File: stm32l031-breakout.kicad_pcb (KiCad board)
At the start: 2 copper layers, 12 parts, among them J1 Conn_01x16, J2 Conn_01x16, U1 STM32L031K6Tx

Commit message: Placement candidate
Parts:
- moved C6 9.09 mm to (143.5, 113.7), turned to 90 degrees
- moved R1 4.62 mm to (143.5, 109.9), turned to 270 degrees
- moved C4 3.64 mm to (146.7, 118.6), turned to 180 degrees
- moved J2 2.54 mm to (139.7, 104.1)
- moved SW_BOOT1 1.91 mm to (146.7, 111.8)
- moved C1 1.42 mm to (152.4, 112.4)
- moved U1 1.42 mm to (160.0, 112.4)
- moved C2 1.42 mm to (167.6, 112.4)
- moved C3 1.28 mm to (154.2, 117.2)
- moved SW_RST1 0.64 mm to (140.3, 111.8), turned to 270 degrees
- moved C5 0.25 mm to (141.0, 119.1)
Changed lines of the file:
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@@
   )
   (module local_footprints:0805_HS (layer F.Cu)
-    (at 151.13 111.76 90)
+    (at 152.4 112.395 90)
     (descr "Resistor SMD 0805, reflow soldering, Vishay (see dcrcw.pdf)")
     (tags "resistor 0805")
@@
   )
   (module local_footprints:0805_HS (layer F.Cu)
-    (at 166.37 111.76 270)
+    (at 167.64 112.395 270)
     (descr "Resistor SMD 0805, reflow soldering, Vishay (see dcrcw.pdf)")
     (tags "resistor 0805")
@@
   )
   (module local_footprints:0805_HS (layer F.Cu)
-    (at 153.213173 116.383173 135)
+    (at 154.178 117.221 135)
     (descr "Resistor SMD 0805, reflow soldering, Vishay (see dcrcw.pdf)")
     (tags "resistor 0805")
@@
   )
   (module local_footprints:1206_HS (layer F.Cu)
-    (at 149.86 116.84 90)
+    (at 146.685 118.618 180)
     (descr "Resistor SMD 1206, reflow soldering, Vishay (see dcrcw.pdf)")
     (tags "resistor 1206")
     (attr smd)
-    (fp_text reference C4 (at 0 0 180) (layer F.SilkS)
+    (fp_text reference C4 (at 0 0 270) (layer F.SilkS)
       (effects (font (size 0.762 0.762) (thickness 0.1016)))
     )
-    (fp_text value 1uF (at 0 1.95 90) (layer F.Fab) hide
+    (fp_text value 1uF (at 0 1.95 180) (layer F.Fab) hide
       (effects (font (size 1 1) (thickness 0.15)))
     )
@@
     (fp_line (start 1.6 0.8) (end -1.6 0.8) (layer F.Fab) (width 0.1))
     (fp_line (start -1.6 0.8) (end -1.6 -0.8) (layer F.Fab) (width 0.1))
-    (fp_text user %R (at 0 0 90) (layer F.Fab)
+    (fp_text user %R (at 0 0 180) (layer F.Fab)
       (effects (font (size 0.7 0.7) (thickness 0.105)))
     )
-    (pad 2 smd roundrect (at 1.65 0 90) (size 1.3 1.7) (layers F.Cu F.Paste F.Mask) (roundrect_rratio 0.25)
-      (net 2 GND))
-    (pad 1 smd roundrect (at -1.65 0 90) (size 1.3 1.7) (layers F.Cu F.Paste F.Mask) (roundrect_rratio 0.25)
+    (pad 2 smd roundrect (at 1.65 0 180) (size 1.3 1.7) (layers F.Cu F.Paste F.Mask) (roundrect_rratio 0.25)
+      (net 2 GND))
+    (pad 1 smd roundrect (at -1.65 0 180) (size 1.3 1.7) (layers F.Cu F.Paste F.Mask) (roundrect_rratio 0.25)
       (net 1 VDD))
     (model ${KISYS3DMOD}/Resistors_SMD.3dshapes/R_1206.wrl
@@
   )
   (module local_footprints:1210_HS (layer F.Cu)
-    (at 140.97 119.38)
+    (at 140.97 119.126)
     (descr "Generic SMD 1210")
     (tags "resistor 1206")
@@
   )
   (module local_footprints:0805_HS (layer F.Cu)
-    (at 139.7 105.41)
+    (at 143.51 113.665 90)
     (descr "Resistor SMD 0805, reflow soldering, Vishay (see dcrcw.pdf)")
     (tags "resistor 0805")
     (attr smd)
-    (fp_text reference C6 (at 0 0 90) (layer F.SilkS)
+    (fp_text reference C6 (at 0 0 180) (layer F.SilkS)
       (effects (font (size 0.635 0.635) (thickness 0.1016)))
     )
-    (fp_text value 0.1uF (at 0 1.75) (layer F.Fab) hide
-      (effects (font (size 1 1) (thickness 0.15)))
-    )
-    (fp_text user %R (at 0 0) (layer F.Fab)
+    (fp_text value 0.1uF (at 0 1.75 90) (layer F.Fab) hide
+      (effects (font (size 1 1) (thickness 0.15)))
+    )
+    (fp_text user %R (at 0 0 90) (layer F.Fab)
       (effects (font (size 0.5 0.5) (thickness 0.075)))
     )
@@
     (fp_line (start 1.55 0.9) (end 1.55 -0.9) (layer F.CrtYd) (width 0.05))
     (fp_line (start 1.55 0.9) (end -1.55 0.9) (layer F.CrtYd) (width 0.05))
-    (pad 1 smd roundrect (at -1.15 0) (size 1.1 1.3) (layers F.Cu F.Paste F.Mask) (roundrect_rratio 0.25)
+    (pad 1 smd roundrect (at -1.15 0 90) (size 1.1 1.3) (layers F.Cu F.Paste F.Mask) (roundrect_rratio 0.25)
       (net 3 "Net-(C6-Pad1)"))
-    (pad 2 smd roundrect (at 1.15 0) (size 1.1 1.3) (layers F.Cu F.Paste F.Mask) (roundrect_rratio 0.25)
+    (pad 2 smd roundrect (at 1.15 0 90) (size 1.1 1.3) (layers F.Cu F.Paste F.Mask) (roundrect_rratio 0.25)
       (net 2 GND))
     (model ${KISYS3DMOD}/Resistors_SMD.3dshapes/R_0805.wrl
@@
   )
   (module local_footprints:Pin_Header_Straight_1x16_Pitch2.54mm (layer F.Cu)
-    (at 139.7 101.6 90)
+    (at 139.7 104.14 90)
     (descr "Through hole straight pin header, 1x16, 2.54mm pitch, single row")
     (tags "Through hole pin header THT 1x16 2.54mm single row")
@@
   )
   (module local_footprints:0805_HS (layer F.Cu)
-    (at 144.78 105.41 180)
+    (at 143.51 109.855 270)
     (descr "Resistor SMD 0805, reflow soldering, Vishay (see dcrcw.pdf)")
     (tags "resistor 0805")
     (attr smd)
-    (fp_text reference R1 (at 0 0 270) (layer F.SilkS)
+    (fp_text reference R1 (at 0 0) (layer F.SilkS)
       (effects (font (size 0.635 0.635) (thickness 0.1016)))
     )
-    (fp_text value 10k (at 0 1.75 180) (layer F.Fab) hide
+    (fp_text value 10k (at 0 1.75 270) (layer F.Fab) hide
       (effects (font (size 1 1) (thickness 0.15)))
     )
@@
     (fp_line (start 1 0.62) (end -1 0.62) (layer F.Fab) (width 0.1))
     (fp_line (start -1 0.62) (end -1 -0.62) (layer F.Fab) (width 0.1))
-    (fp_text user %R (at 0 0 180) (layer F.Fab)
+    (fp_text user %R (at 0 0 270) (layer F.Fab)
       (effects (font (size 0.5 0.5) (thickness 0.075)))
     )
-    (pad 2 smd roundrect (at 1.15 0 180) (size 1.1 1.3) (layers F.Cu F.Paste F.Mask) (roundrect_rratio 0.25)
-      (net 2 GND))
-    (pad 1 smd roundrect (at -1.15 0 180) (size 1.1 1.3) (layers F.Cu F.Paste F.Mask) (roundrect_rratio 0.25)
+    (pad 2 smd roundrect (at 1.15 0 270) (size 1.1 1.3) (layers F.Cu F.Paste F.Mask) (roundrect_rratio 0.25)
+      (net 2 GND))
+    (pad 1 smd roundrect (at -1.15 0 270) (size 1.1 1.3) (layers F.Cu F.Paste F.Mask) (roundrect_rratio 0.25)
       (net 29 BOOT))
     (model ${KISYS3DMOD}/Resistors_SMD.3dshapes/R_0805.wrl
@@
   )
   (module local_footprints:SW_SPST_PUSH_6mm_3mm (layer F.Cu)
-    (at 144.78 111.76 270)
+    (at 146.685 111.76 270)
     (descr http://www.te.com/commerce/DocumentDelivery/DDEController?Action=srchrtrv&DocNm=1437566-3&DocType=Customer+Drawing&DocLang=English)
     (tags "SPST button tactile switch")
@@
   )
   (module local_footprints:SW_SPST_PUSH_6mm_3mm (layer F.Cu)
-    (at 139.7 111.76 90)
+    (at 140.335 111.76 270)
     (descr http://www.te.com/commerce/DocumentDelivery/DDEController?Action=srchrtrv&DocNm=1437566-3&DocType=Customer+Drawing&DocLang=English)
     (tags "SPST button tactile switch")
     (attr smd)
-    (fp_text reference SW_RST1 (at 0 0 90) (layer F.SilkS)
-      (effects (font (size 1 1) (thickness 0.15)))
-    )
-    (fp_text value SW_RST (at 0 3 90) (layer F.Fab)
+    (fp_text reference SW_RST1 (at 0 0 270) (layer F.SilkS)
+      (effects (font (size 1 1) (thickness 0.15)))
+    )
+    (fp_text value SW_RST (at 0 3 270) (layer F.Fab)
       (effects (font (size 1 1) (thickness 0.15)))
     )
@@
     (fp_line (start 1.75 -1) (end 1.75 1) (layer F.Fab) (width 0.1))
     (fp_line (start -1.75 -1) (end 1.75 -1) (layer F.Fab) (width 0.1))
-    (fp_text user %R (at 0 -2.6 90) (layer F.Fab)
-      (effects (font (size 1 1) (thickness 0.15)))
-    )
-    (pad 2 smd roundrect (at 3.9 0 90) (size 2 1.6) (layers F.Cu F.Paste F.Mask) (roundrect_rratio 0.25)
+    (fp_text user %R (at 0 -2.6 270) (layer F.Fab)
+      (effects (font (size 1 1) (thickness 0.15)))
+    )
+    (pad 2 smd roundrect (at 3.9 0 270) (size 2 1.6) (layers F.Cu F.Paste F.Mask) (roundrect_rratio 0.25)
       (net 3 "Net-(C6-Pad1)"))
-    (pad 1 smd roundrect (at -3.9 0 90) (size 2 1.6) (layers F.Cu F.Paste F.Mask) (roundrect_rratio 0.25)
+    (pad 1 smd roundrect (at -3.9 0 270) (size 2 1.6) (layers F.Cu F.Paste F.Mask) (roundrect_rratio 0.25)
       (net 2 GND))
     (model ${KISYS3DMOD}/Buttons_Switches_SMD.3dshapes/SW_SPST_FSMSM.wrl
@@
   )
   (module local_footprints:TQFP-32_7x7mm_Pitch0.8mm_HS_narrow_pads (layer F.Cu)
-    (at 158.75 111.76 45)
+    (at 160.02 112.395 45)
     (descr "32-Lead Plastic Thin Quad Flatpack (PT) - 7x7x1.0 mm Body, 2.00 mm [TQFP] (see Microchip Packaging Specification 00000049BS.pdf)")
     (tags "QFP 0.8")

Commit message: Full layout
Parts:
- moved C4 2.83 mm to (149.5, 118.2)
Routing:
- net VDD: track 0.00 -> 46.4 mm
- net Net-(C6-Pad1): track 0.00 -> 21.0 mm, vias 0 -> 2
- net GND: track 0.00 -> 20.1 mm, vias 0 -> 9
- net PB1: track 0.00 -> 16.5 mm
- net PB7: track 0.00 -> 16.3 mm
- net PA8: track 0.00 -> 16.0 mm
- net PC14: track 0.00 -> 14.9 mm, vias 0 -> 2
- net PB0: track 0.00 -> 14.3 mm
- net PB6: track 0.00 -> 14.1 mm
- net PA9.SCL.TX: track 0.00 -> 13.8 mm
- net BOOT: track 0.00 -> 13.5 mm
- net PC15: track 0.00 -> 12.7 mm, vias 0 -> 2
- net PB5: track 0.00 -> 11.9 mm
- net PA10.SDA.RX: track 0.00 -> 11.6 mm
- net PA0: track 0.00 -> 10.5 mm
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- added copper zone on B.Cu, net GND
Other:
- board outline added: 40.6 x 20.3 mm

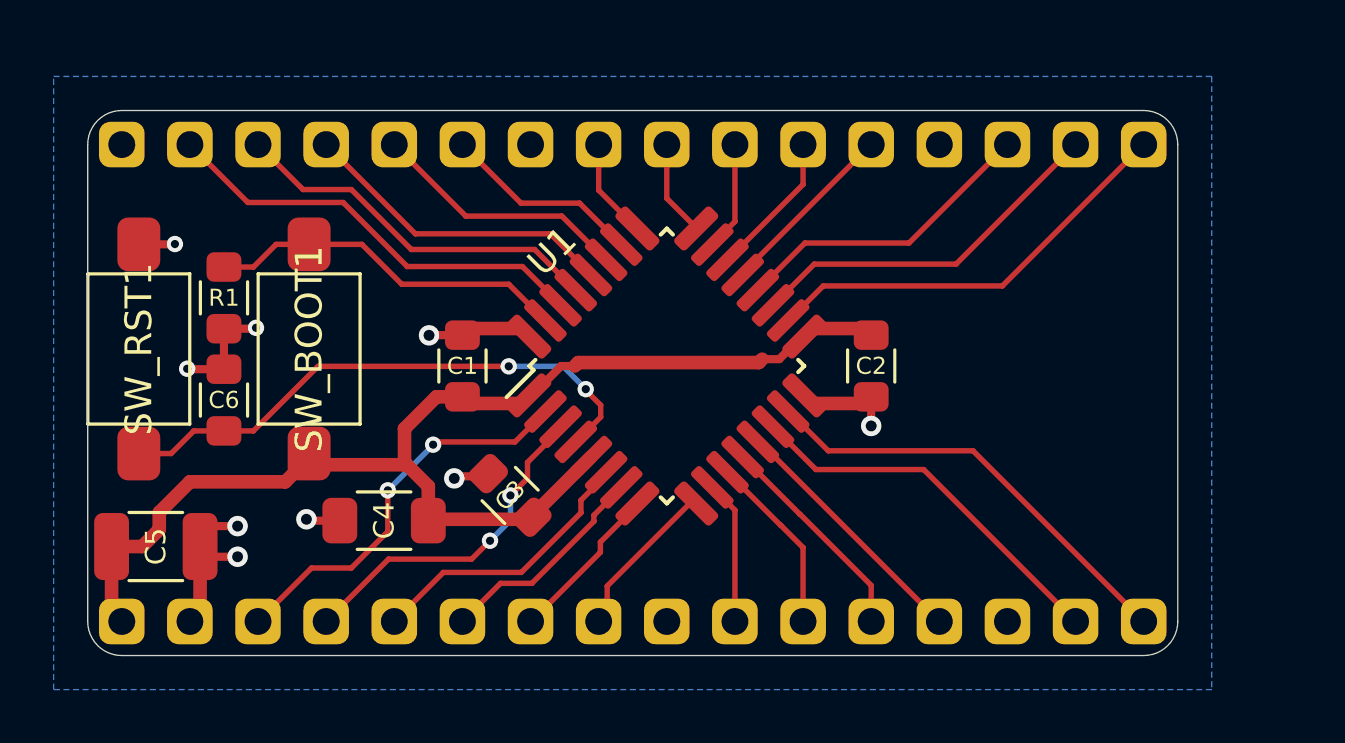
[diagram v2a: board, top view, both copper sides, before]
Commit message: Added optional battery connector and 2V5 regulator
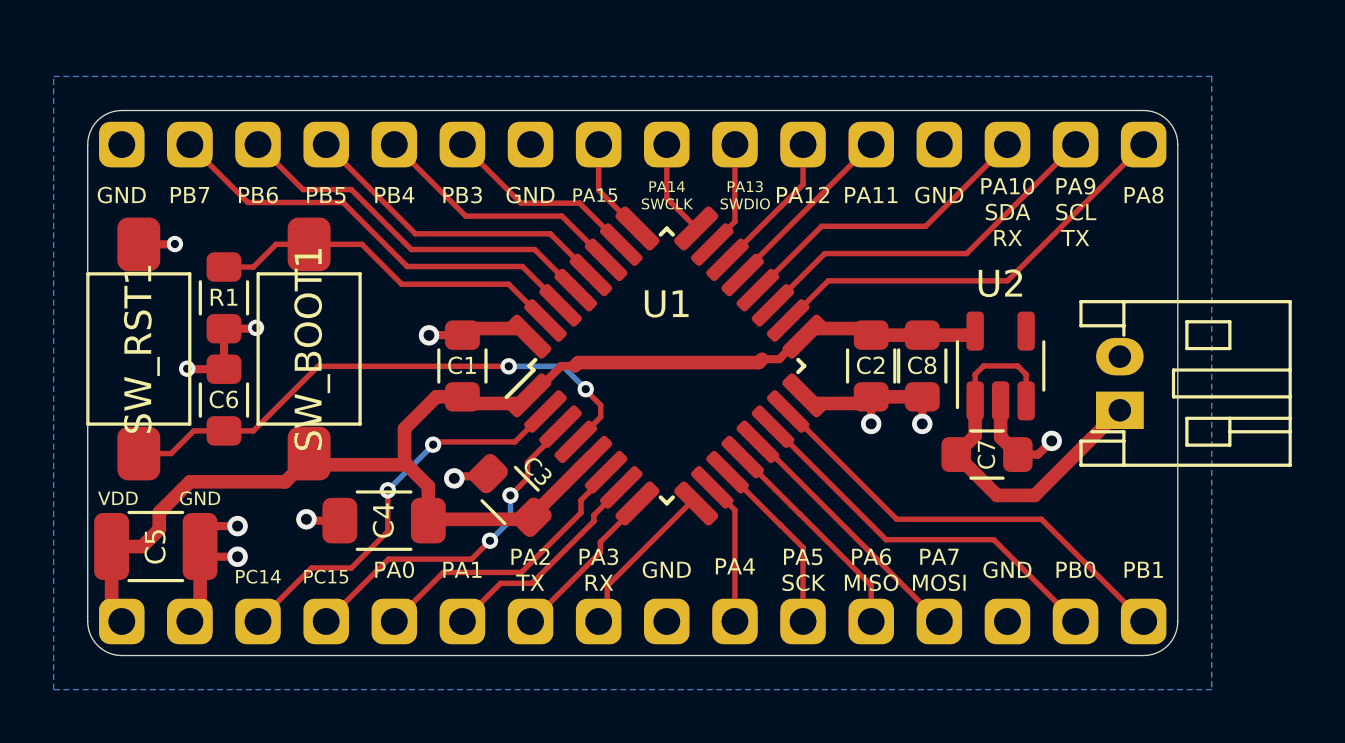
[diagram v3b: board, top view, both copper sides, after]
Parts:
- added C7: 0.1u, local_footprints:0805_HS, F.Cu at (172.0, 115.7)
- added C8: 0.1u, local_footprints:0805_HS, F.Cu at (169.5, 112.4)
- added J3: JST_PH, local_footprints:JST_PH_S2B-PH-K_02x2.00mm_Angled_WiderHole, F.Cu at (176.9, 114.0)
- added U2: AP7354, local_footprints:SOT-23-5_HS, F.Cu at (172.5, 112.4)
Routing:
- net Net-(C7-Pad2): track 0.00 -> 14.5 mm
- net GND: track 20.1 -> 26.8 mm, vias 9 -> 11
- net VDD: track 46.4 -> 50.3 mm
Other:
- board text added: "GND"
- board text added: "PA0"
- board text added: "PA1"
- board text added: "PA10 SDA RX"
- board text added: "PA11"
- board text added: "PA12"
- board text added: "PA13 SWDIO"
- board text added: "PA14 SWCLK"
- board text added: "PA15"
- board text added: "PA2 TX"
- board text added: "PA3 RX"
- board text added: "PA4"
- board text added: "PA5 SCK"
- board text added: "PA6 MISO"
- board text added: "PA7 MOSI"
- board text added: "PA8"
- board text added: "PA9 SCL TX"
- board text added: "PB0"
- board text added: "PB1"
- board text added: "PB3"
- board text added: "PB4"
- board text added: "PB5"
- board text added: "PB6"
- board text added: "PB7"
- board text added: "PC14"
- board text added: "PC15"
- board text added: "VDD"

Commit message: Complete design and layout
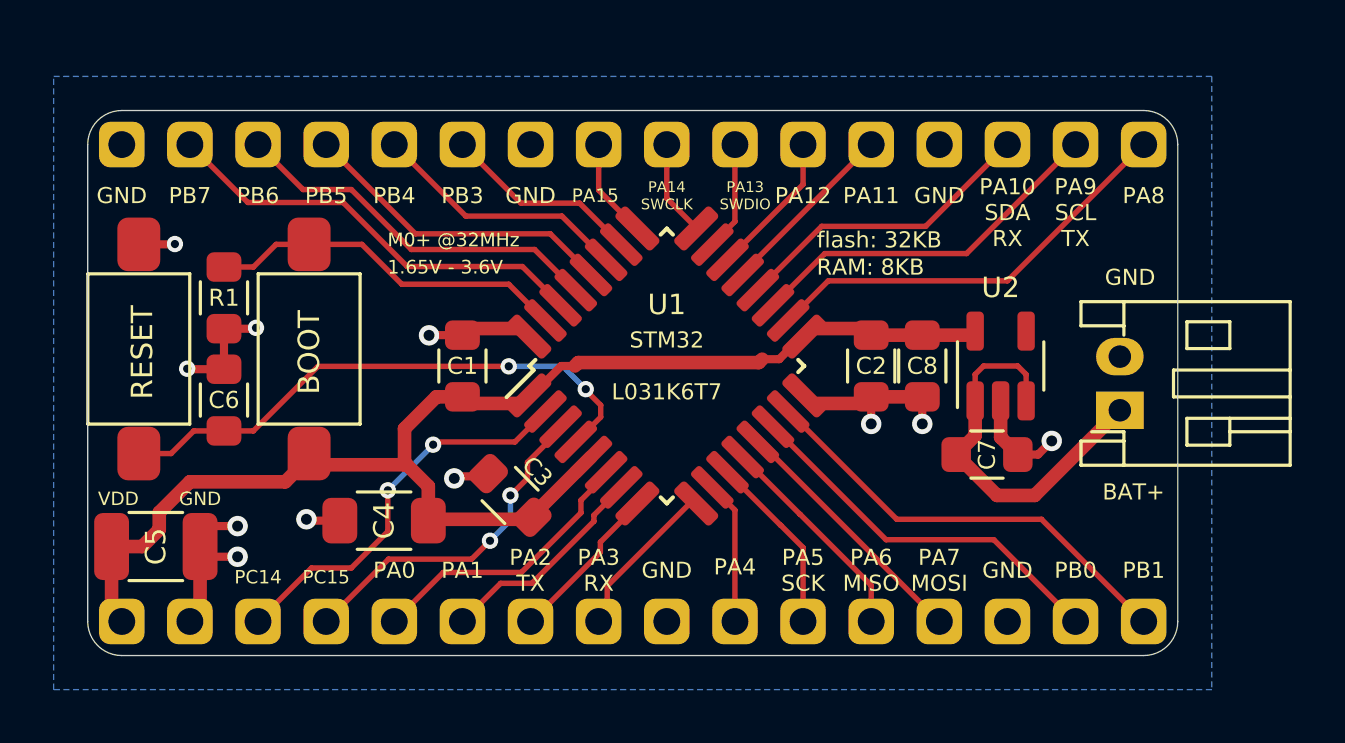
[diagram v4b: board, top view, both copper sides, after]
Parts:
- added REF***: OSHW-Logo2_7.3x6mm_SilkScreen, Symbols:OSHW-Logo2_7.3x6mm_SilkScreen, B.Cu at (145.3, 114.6)
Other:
- rule pad_to_mask_clearance: 0.051 -> 0.0254
- rule solder_mask_min_width: 0.25 -> 0.1524
- board text added: "(C) Vlad Belous"
- board text added: "1.65V - 3.6V"
- board text added: "BAT+"
- board text added: "BOOT"
- board text added: "CC BY-SA 4.0"
- board text added: "M0+ @32MHz"
- board text added: "NOTES:"
- board text added: "RAM: 8KB"
- board text added: "RESET"
- board text added: "STM32 L031K6T7"
- board text added: "flash: 32KB"
